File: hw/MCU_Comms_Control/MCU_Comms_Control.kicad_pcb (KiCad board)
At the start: 4 copper layers, 72.1 x 97 mm, 62 parts, among them J1 USB_B_Mini, J2 CAN BUS, J3 TO_POWER_BOARD, J4 Mini-Debugging, J5 MULTI, J6 TEMP, J7 CAN, SW1 BOOT, SW2 BUTTON, U1 SRV05-4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

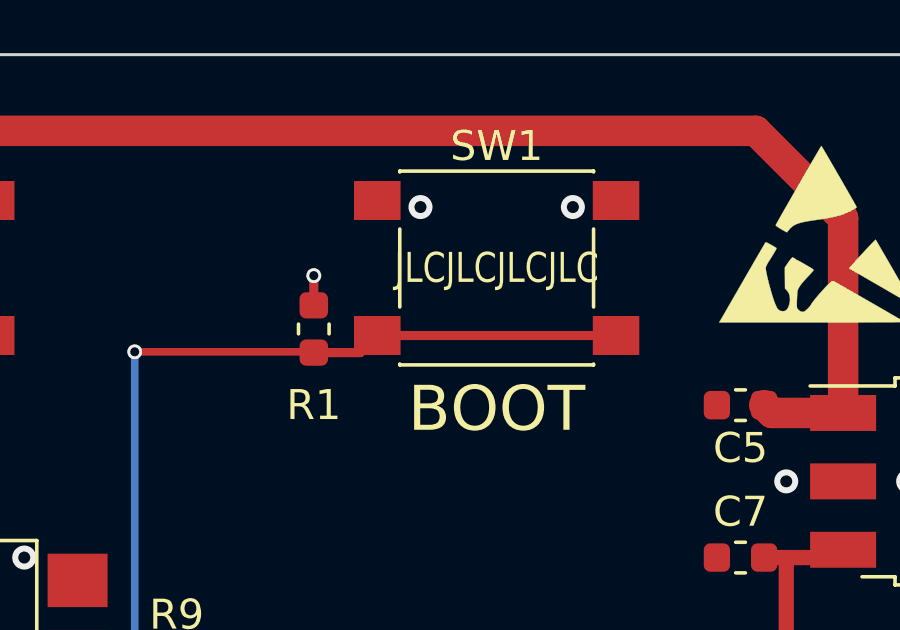
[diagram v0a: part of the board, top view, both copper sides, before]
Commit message: fix boot0 resistor
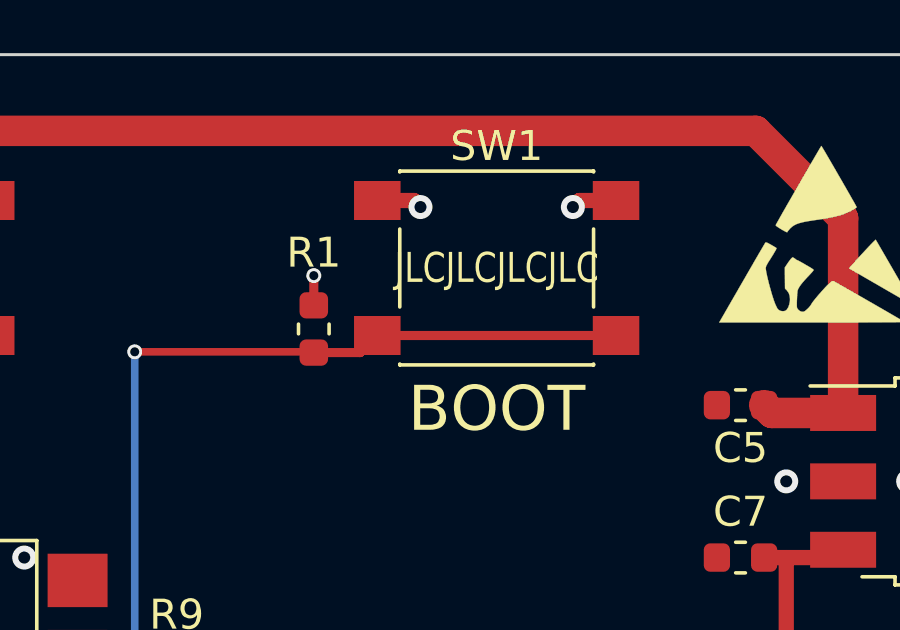
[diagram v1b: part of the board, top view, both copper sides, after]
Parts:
- turned R1 to 270 degrees
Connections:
- R1 pad 1: ~BOOT -> GND
- R1 pad 2: +3V3 -> ~BOOT
- SW1 pad 2: GND -> +3V3
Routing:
- net +3V3: track 58.4 -> 60.5 mm, vias 19 -> 20
- net GND: track 16.7 -> 17.7 mm, vias 52 -> 51

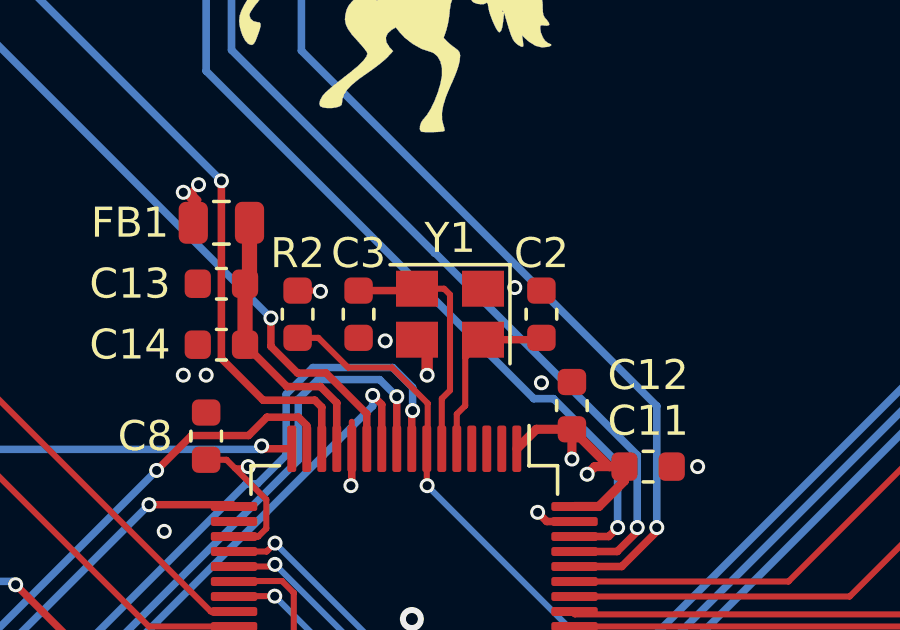
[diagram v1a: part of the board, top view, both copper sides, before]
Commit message: tag wrong crystal footprint
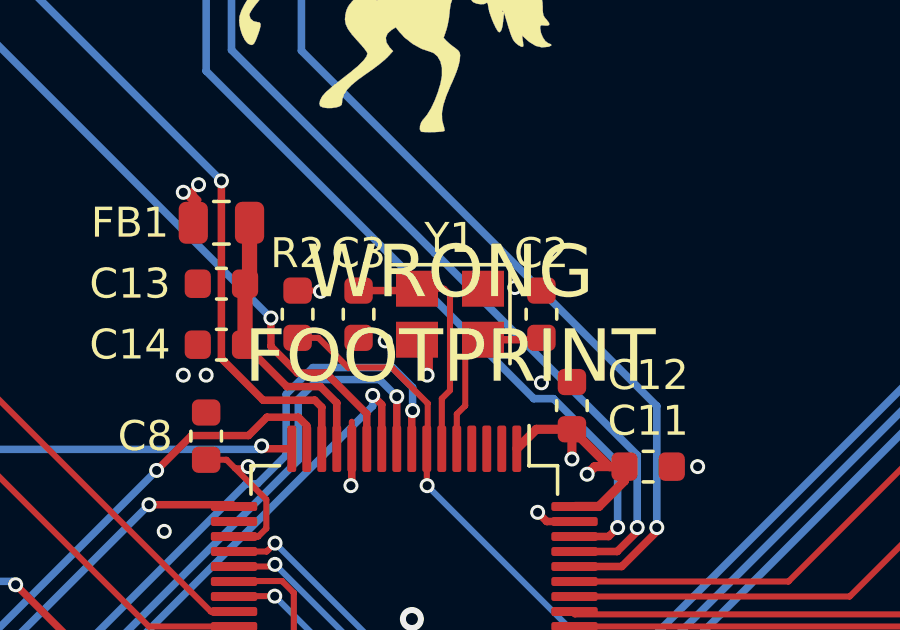
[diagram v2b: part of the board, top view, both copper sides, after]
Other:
- board text added: "WRONG FOOTPRINT"

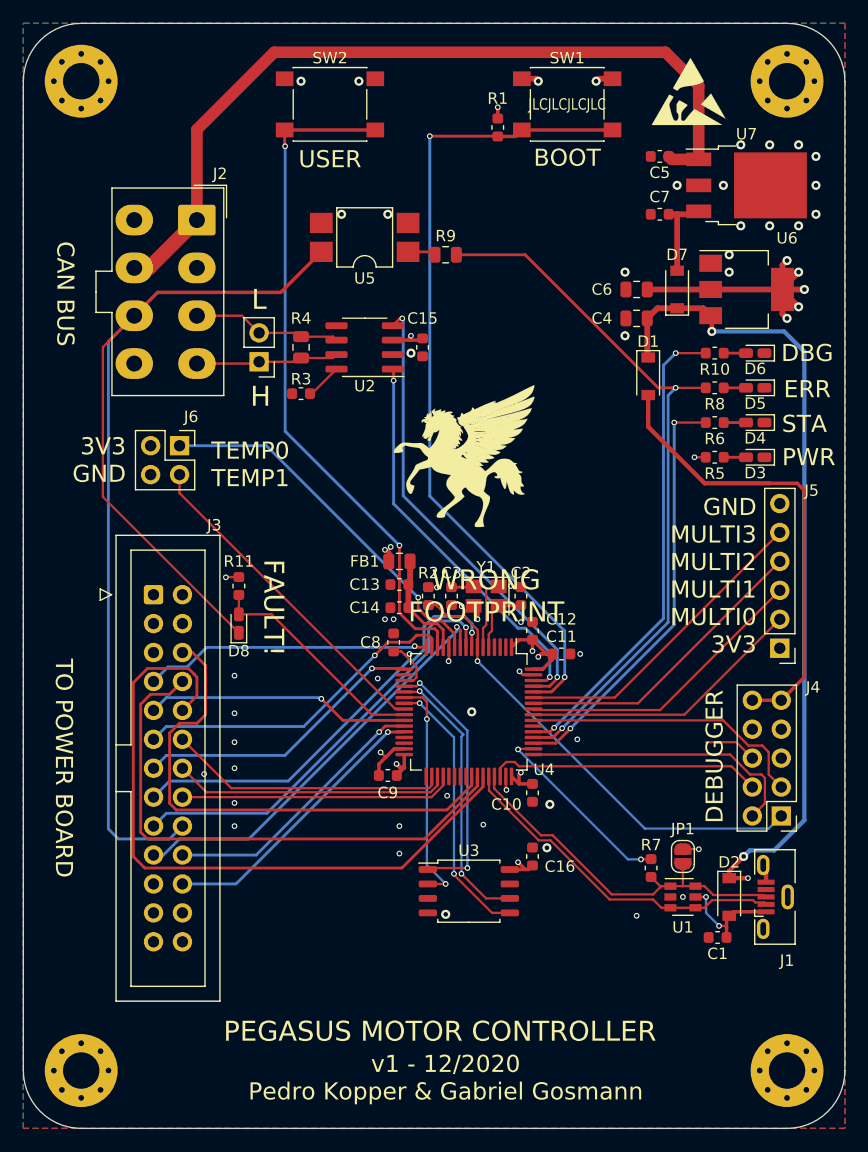
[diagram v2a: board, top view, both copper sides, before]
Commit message: mini-fit (CAN) connector hole size from 1.4 to 1.8mm diameter and add silkscreen labels for the debugger pins
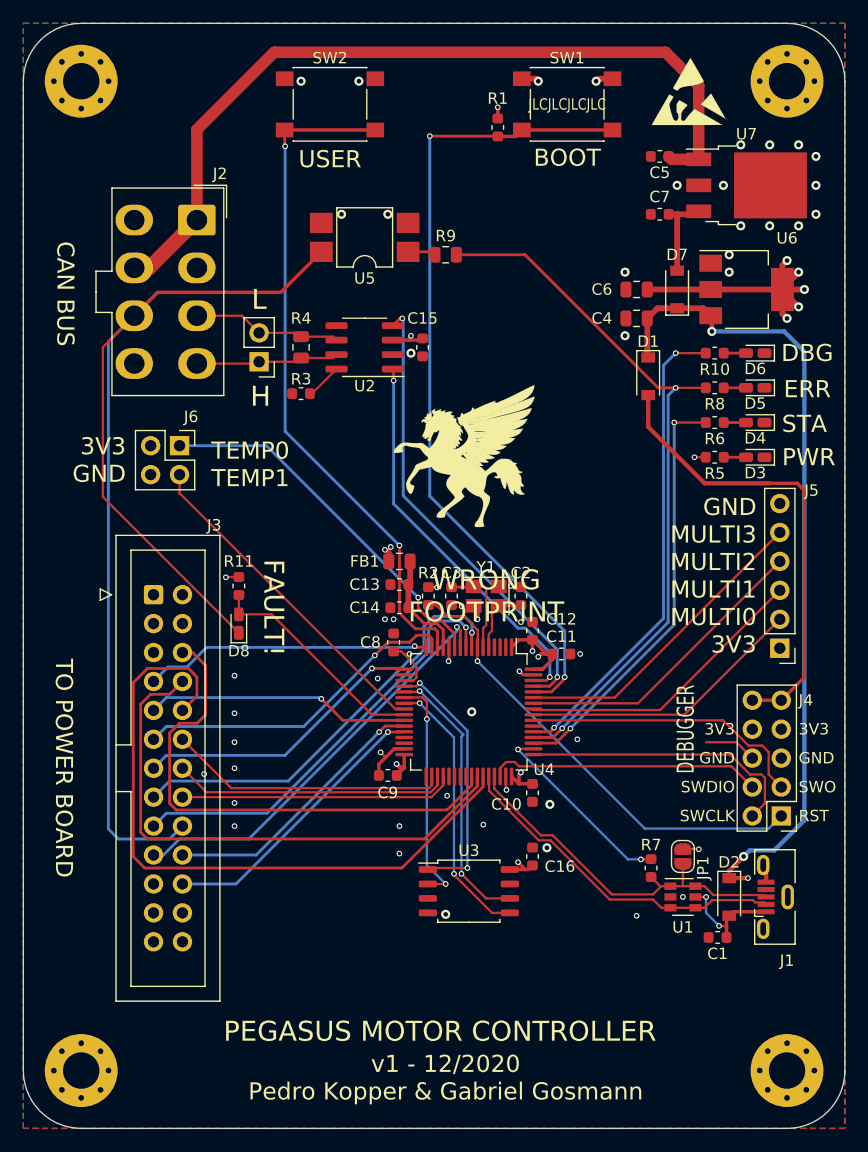
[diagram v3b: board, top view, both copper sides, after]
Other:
- board text added: "3V3"
- board text added: "GND"
- board text added: "RST"
- board text added: "SWCLK"
- board text added: "SWDIO"
- board text added: "SWO"
